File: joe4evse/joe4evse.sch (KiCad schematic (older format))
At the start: 41 parts, among them J1 USB_B_Micro, J10 Conn_01x02, J11 Conn_01x02, J12 Conn_02x06_Odd_Even, J14 Conn_01x02, J2 Conn_01x03, J3 Conn_01x03, J4 Conn_01x02, J5 Conn_01x03, J6 CONNFLY_Elec_DS1129-04-S8B0P-X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

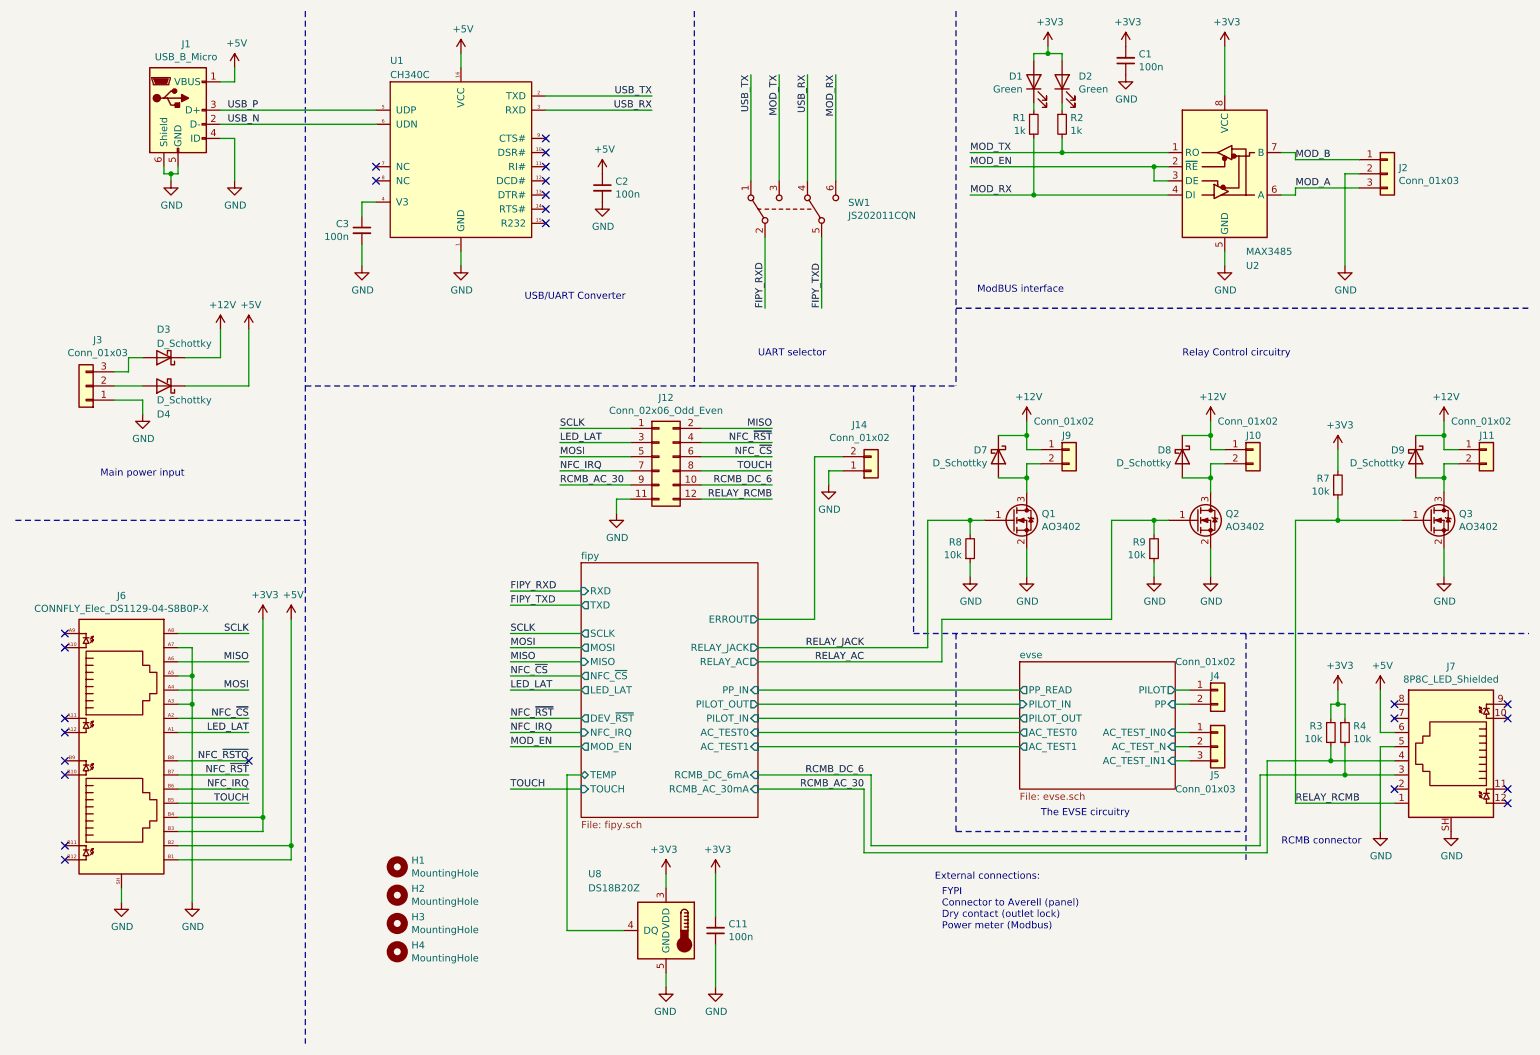
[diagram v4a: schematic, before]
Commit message: joe/{sch, pcb}: Combine AC_RELAY and RCMB output
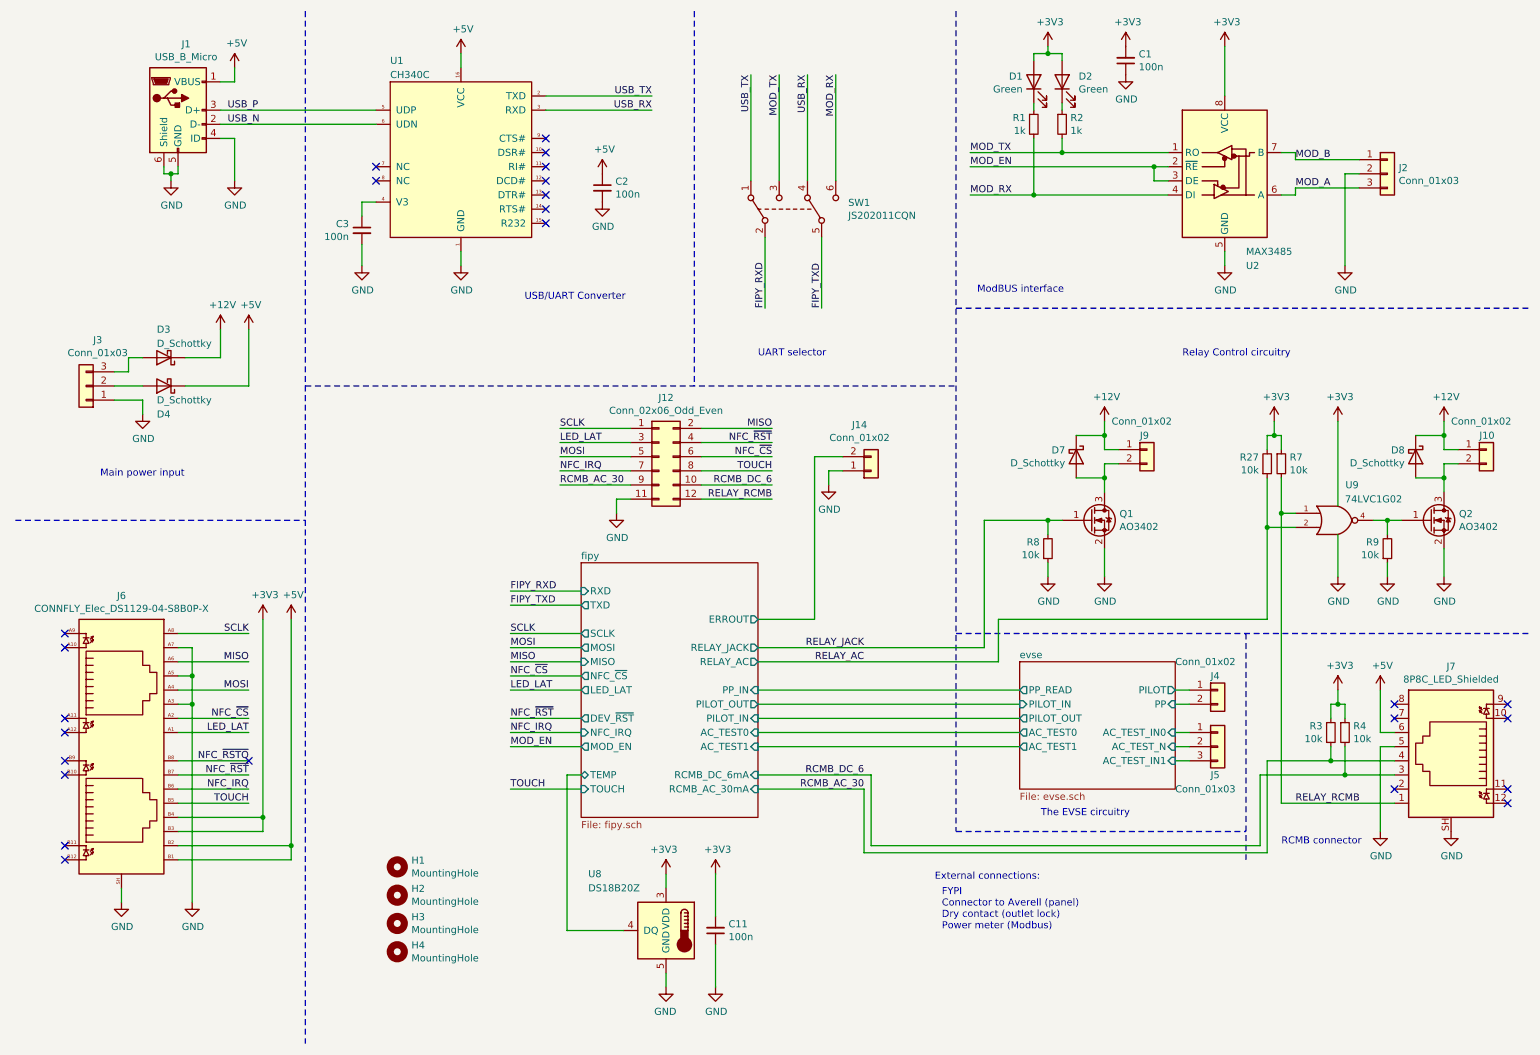
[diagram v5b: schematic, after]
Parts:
- removed D9: D_Schottky, Diode_SMD:D_SOD-123, symbol Device:D_Schottky
- removed J11: Conn_01x02, Connector_JST:JST_PH_B2B-PH-K_1x02_P2.00mm_Vertical, symbol Connector_Generic:Conn_01x02
- removed Q3: AO3402, Package_TO_SOT_SMD:SOT-23, symbol ma4evse:AO3402
- added R27: 10k, Resistor_SMD:R_0603_1608Metric, symbol Device:R_Small
- added U9: 74LVC1G02, Package_TO_SOT_SMD:SOT-353_SC-70-5, symbol 74xGxx:74LVC1G02
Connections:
- net +3V3: now also R7.1, R27.2, U9.5 (VCC); no longer R7.2
- net GND: now also U9.3 (GND)
- net RELAY_AC: now also R27.1, U9.2; no longer Q2.1 (G), R9.2
- net RELAY_RCMB: now also R7.2, U9.1; no longer R7.1
- new net: Q2.1 (G), R9.2, U9.4
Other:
- moved on the sheet: D7, D8, J10, J9, Q1, Q2, R7, R8, R9

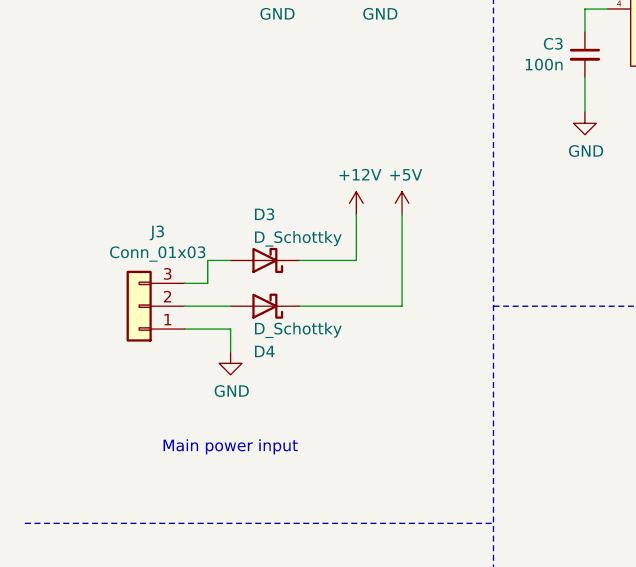
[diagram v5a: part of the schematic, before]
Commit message: joe/{sch, pcb}: Remove input shottky diodes
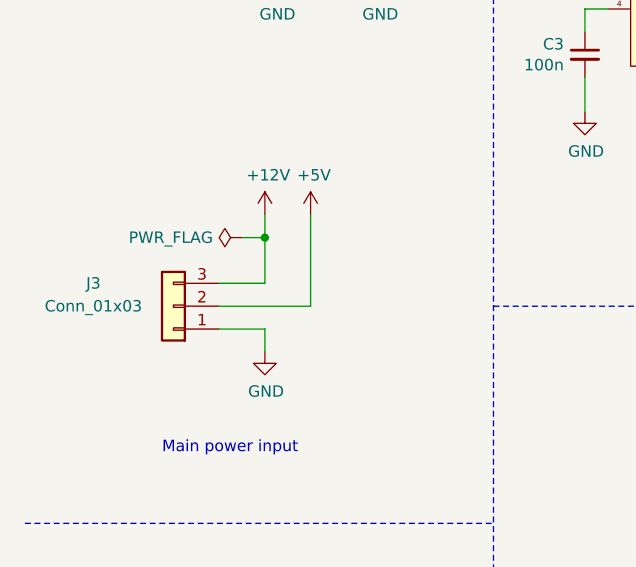
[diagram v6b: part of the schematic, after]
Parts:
- removed D3, D4: D_Schottky, Diode_SMD:D_SOD-123, symbol Device:D_Schottky
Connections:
- net +12V: now also J3.3 (Pin_3)
- net +5V: now also J3.2 (Pin_2)
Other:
- moved on the sheet: J3
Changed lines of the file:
@@
 L power:+5V #PWR016
 U 1 1 5D27C44A
-P 2150 2750
-F 0 "#PWR016" H 2150 2600 50  0001 C CNN
-F 1 "+5V" H 2165 2923 50  0000 C CNN
-F 2 "" H 2150 2750 50  0001 C CNN
-F 3 "" H 2150 2750 50  0001 C CNN
-	1    2150 2750
-	1    0    0    -1
-$EndComp
-Wire Wire Line
-	1200 3150 1400 3150
-Wire Wire Line
-	2150 3150 2150 2750
+P 1750 2750
+F 0 "#PWR016" H 1750 2600 50  0001 C CNN
+F 1 "+5V" H 1765 2923 50  0000 C CNN
+F 2 "" H 1750 2750 50  0001 C CNN
+F 3 "" H 1750 2750 50  0001 C CNN
+	1    1750 2750
+	1    0    0    -1
+$EndComp
 $Comp
 L power:GND #PWR017
 U 1 1 5D27C4DB
-P 1400 3350
-F 0 "#PWR017" H 1400 3100 50  0001 C CNN
-F 1 "GND" H 1405 3177 50  0000 C CNN
-F 2 "" H 1400 3350 50  0001 C CNN
-F 3 "" H 1400 3350 50  0001 C CNN
-	1    1400 3350
-	1    0    0    -1
-$EndComp
-Wire Wire Line
-	1200 3250 1400 3250
-Wire Wire Line
-	1400 3250 1400 3350
+P 1550 3350
+F 0 "#PWR017" H 1550 3100 50  0001 C CNN
+F 1 "GND" H 1555 3177 50  0000 C CNN
+F 2 "" H 1550 3350 50  0001 C CNN
+F 3 "" H 1550 3350 50  0001 C CNN
+	1    1550 3350
+	1    0    0    -1
+$EndComp
+Wire Wire Line
+	1350 3250 1550 3250
+Wire Wire Line
+	1550 3250 1550 3350
 Text Notes 1100 3800 0    50   ~ 0
 Main power input
@@
 	1    0    0    -1
 $EndComp
-$Comp
-L Device:D_Schottky D4
-U 1 1 5D4319B1
-P 1550 3150
-F 0 "D4" H 1600 3350 50  0000 R CNN
-F 1 "D_Schottky" H 1600 3250 50  0000 R CNN
-F 2 "Diode_SMD:D_SOD-123" H 1550 3150 50  0001 C CNN
-F 3 "~" H 1550 3150 50  0001 C CNN
-	1    1550 3150
-	-1   0    0    1
-$EndComp
-Wire Wire Line
-	1700 3150 2150 3150
 Wire Notes Line
 	5300 500  5300 3150
@@
 L Connector_Generic:Conn_01x03 J3
 U 1 1 5E273351
-P 1000 3150
-F 0 "J3" H 918 2825 50  0000 C CNN
-F 1 "Conn_01x03" H 918 2916 50  0000 C CNN
-F 2 "Connector_JST:JST_EH_B3B-EH-A_1x03_P2.50mm_Vertical" H 1000 3150 50  0001 C CNN
-F 3 "~" H 1000 3150 50  0001 C CNN
-	1    1000 3150
+P 1150 3150
+F 0 "J3" H 1500 3050 50  0000 C CNN
+F 1 "Conn_01x03" H 1500 3150 50  0000 C CNN
+F 2 "Connector_JST:JST_EH_B3B-EH-A_1x03_P2.50mm_Vertical" H 1150 3150 50  0001 C CNN
+F 3 "~" H 1150 3150 50  0001 C CNN
+	1    1150 3150
 	-1   0    0    1
 $EndComp
-$Comp
-L Device:D_Schottky D3
-U 1 1 5E2741F8
-P 1550 2950
-F 0 "D3" H 1600 2750 50  0000 R CNN
-F 1 "D_Schottky" H 1600 2850 50  0000 R CNN
-F 2 "Diode_SMD:D_SOD-123" H 1550 2950 50  0001 C CNN
-F 3 "~" H 1550 2950 50  0001 C CNN
-	1    1550 2950
-	-1   0    0    1
-$EndComp
-Wire Wire Line
-	1200 3050 1300 3050
-Wire Wire Line
-	1300 3050 1300 2950
-Wire Wire Line
-	1300 2950 1400 2950
-Wire Wire Line
-	1700 2950 1950 2950
-Wire Wire Line
-	1950 2950 1950 2750
+Wire Wire Line
+	1550 3050 1550 2850
 $Comp
 L power:+12V #PWR015
 U 1 1 5E28A95B
-P 1950 2750
-F 0 "#PWR015" H 1950 2600 50  0001 C CNN
-F 1 "+12V" H 1965 2923 50  0000 C CNN
-F 2 "" H 1950 2750 50  0001 C CNN
-F 3 "" H 1950 2750 50  0001 C CNN
-	1    1950 2750
+P 1550 2750
+F 0 "#PWR015" H 1550 2600 50  0001 C CNN
+F 1 "+12V" H 1565 2923 50  0000 C CNN
+F 2 "" H 1550 2750 50  0001 C CNN
+F 3 "" H 1550 2750 50  0001 C CNN
+	1    1550 2750
 	1    0    0    -1
 $EndComp
@@
 Wire Wire Line
 	9450 4050 9450 6100
+Wire Wire Line
+	1350 3150 1750 3150
+Wire Wire Line
+	1350 3050 1550 3050
+$Comp
+L power:PWR_FLAG #FLG0101
+U 1 1 603D27CA
+P 1450 2850
+F 0 "#FLG0101" H 1450 2925 50  0001 C CNN
+F 1 "PWR_FLAG" V 1450 2977 50  0000 L CNN
+F 2 "" H 1450 2850 50  0001 C CNN
+F 3 "~" H 1450 2850 50  0001 C CNN
+	1    1450 2850
+	0    -1   -1   0
+$EndComp
+Wire Wire Line
+	1450 2850 1550 2850
+Connection ~ 1550 2850
+Wire Wire Line
+	1550 2850 1550 2750
+Wire Wire Line
+	1750 2750 1750 3150
 $EndSCHEMATC

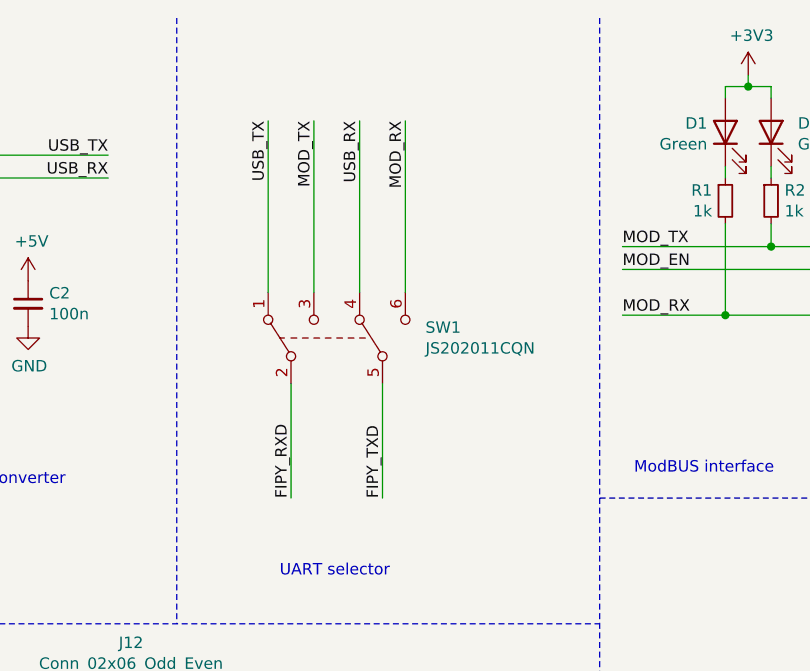
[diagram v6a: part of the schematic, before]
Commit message: joe/{sch, pcb}: Add 0r resistors in parallel of SW1 for prod boards
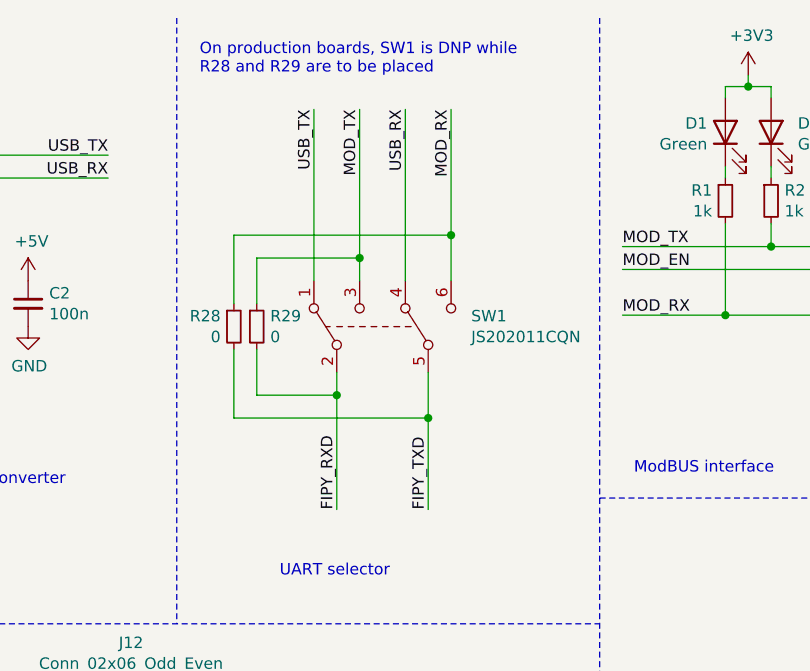
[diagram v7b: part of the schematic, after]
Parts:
- added R28, R29: 0, Resistor_SMD:R_0603_1608Metric, symbol Device:R_Small
- J1: Manufacturer (none) -> Molex; Manufacturer PN (none) -> 47346-0001
- J10, J14, J2, J3, J4, J5, J9: Manufacturer (none) -> JST
- U1: Manufacturer (none) -> WCH; Manufacturer PN (none) -> CH340C
- U2: Manufacturer (none) -> Maxim; Manufacturer PN (none) -> MAX3485
- U8: Manufacturer (none) -> Maxim
- U9: Manufacturer (none) -> Ti
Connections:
- net FIPY_RXD: now also R29.2
- net FIPY_TXD: now also R28.2
- net MOD_RX: now also R28.1
- net MOD_TX: now also R29.1
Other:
- note added: "On production boards, SW1 is DNP while\nR28 and R29 are to be placed"
- moved on the sheet: SW1
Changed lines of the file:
@@
 F 2 "Package_SO:SOIC-8_3.9x4.9mm_P1.27mm" H 9050 900 50  0001 C CNN
 F 3 "https://datasheets.maximintegrated.com/en/ds/MAX3483-MAX3491.pdf" H 9050 1650 50  0001 C CNN
+F 4 "Maxim" H 9050 1600 50  0001 C CNN "Manufacturer"
+F 5 "MAX3485" H 9050 1600 50  0001 C CNN "Manufacturer PN"
 	1    9050 1600
 	1    0    0    -1
@@
 F 2 "Connector_USB:USB_Micro-B_Molex_47346-0001" H 1800 1150 50  0001 C CNN
 F 3 "~" H 1800 1150 50  0001 C CNN
+F 4 "Molex" H 1650 1200 50  0001 C CNN "Manufacturer"
+F 5 "47346-0001" H 1650 1200 50  0001 C CNN "Manufacturer PN"
 	1    1650 1200
 	1    0    0    -1
@@
 F 2 "Package_SO:SOIC-16_3.9x9.9mm_P1.27mm" H 4050 -550 50  0001 C CNN
 F 3 "https://cdn.sparkfun.com/datasheets/Dev/Arduino/Other/CH340DS1.PDF" H 3150 1150 50  0001 C CNN
+F 4 "WCH" H 3150 1000 50  0001 C CNN "Manufacturer"
+F 5 "CH340C" H 3150 1000 50  0001 C CNN "Manufacturer PN"
 	1    3150 1000
 	1    0    0    -1
@@
 F 2 "Connector_JST:JST_EH_B3B-EH-A_1x03_P2.50mm_Vertical" H 1150 3150 50  0001 C CNN
 F 3 "~" H 1150 3150 50  0001 C CNN
+F 4 "JST" H 1150 3150 50  0001 C CNN "Manufacturer"
 	1    1150 3150
 	-1   0    0    1
@@
 F 2 "Connector_JST:JST_PH_B2B-PH-K_1x02_P2.00mm_Vertical" H 9000 5300 50  0001 C CNN
 F 3 "~" H 9000 5300 50  0001 C CNN
+F 4 "JST" H 9000 5300 50  0001 C CNN "Manufacturer"
 	1    9000 5300
 	1    0    0    -1
@@
 L ma4evse:JS202011CQN SW1
 U 1 1 5E1C964F
-P 6000 1900
-F 0 "SW1" V 6046 1512 50  0000 R CNN
-F 1 "JS202011CQN" V 5955 1512 50  0000 R CNN
-F 2 "ma4evse:JS202011CQN" H 6000 2100 50  0001 C CNN
-F 3 "~" H 6000 2100 50  0001 C CNN
-	1    6000 1900
+P 6200 1850
+F 0 "SW1" V 6246 1462 50  0000 R CNN
+F 1 "JS202011CQN" V 6155 1462 50  0000 R CNN
+F 2 "ma4evse:JS202011CQN" H 6200 2050 50  0001 C CNN
+F 3 "~" H 6200 2050 50  0001 C CNN
+	1    6200 1850
 	0    -1   -1   0
 $EndComp
 Wire Wire Line
-	6200 2100 6200 2600
-Wire Wire Line
-	5800 2100 5800 2600
-Text Label 5800 2600 1    50   ~ 0
+	6400 2050 6400 2250
+Wire Wire Line
+	6000 2050 6000 2150
+Text Label 6000 2650 1    50   ~ 0
 FIPY_RXD
-Text Label 6200 2600 1    50   ~ 0
+Text Label 6400 2650 1    50   ~ 0
 FIPY_TXD
 Wire Wire Line
-	5700 1700 5700 950
-Text Label 5700 950  3    50   ~ 0
+	5900 1650 5900 900
+Text Label 5900 900  3    50   ~ 0
 USB_TX
 Wire Wire Line
-	6100 1700 6100 950
-Text Label 6100 950  3    50   ~ 0
+	6300 1650 6300 900
+Text Label 6300 900  3    50   ~ 0
 USB_RX
 Wire Wire Line
-	5900 1700 5900 950
-Text Label 5900 950  3    50   ~ 0
+	6100 1650 6100 1550
+Text Label 6100 900  3    50   ~ 0
 MOD_TX
 Wire Wire Line
-	6300 1700 6300 950
-Text Label 6300 950  3    50   ~ 0
+	6500 1650 6500 1450
+Text Label 6500 900  3    50   ~ 0
 MOD_RX
 Wire Wire Line
@@
 F 2 "Connector_JST:JST_PH_B2B-PH-K_1x02_P2.00mm_Vertical" H 10900 3600 50  0001 C CNN
 F 3 "~" H 10900 3600 50  0001 C CNN
+F 4 "JST" H 10900 3600 50  0001 C CNN "Manufacturer"
 	1    10900 3600
 	1    0    0    -1
@@
 F 2 "Connector_JST:JST_PH_B2B-PH-K_1x02_P2.00mm_Vertical" H 8500 3600 50  0001 C CNN
 F 3 "~" H 8500 3600 50  0001 C CNN
+F 4 "JST" H 8500 3600 50  0001 C CNN "Manufacturer"
 	1    8500 3600
 	1    0    0    -1
@@
 F 2 "Connector_JST:JST_NV_B03P-NV_1x03_P5.00mm_Vertical" H 9000 5700 50  0001 C CNN
 F 3 "~" H 9000 5700 50  0001 C CNN
+F 4 "JST" H 9000 5700 50  0001 C CNN "Manufacturer"
 	1    9000 5700
 	1    0    0    -1
@@
 F 2 "Package_SO:SOIC-8_3.9x4.9mm_P1.27mm" H 4100 6750 50  0001 C CNN
 F 3 "http://datasheets.maximintegrated.com/en/ds/DS18B20.pdf" H 4950 7250 50  0001 C CNN
+F 4 "Maxim" H 5100 7000 50  0001 C CNN "Manufacturer"
 	1    5100 7000
 	-1   0    0    -1
@@
 F 2 "Connector_JST:JST_PH_B3B-PH-K_1x03_P2.00mm_Vertical" H 10200 1650 50  0001 C CNN
 F 3 "~" H 10200 1650 50  0001 C CNN
+F 4 "JST" H 10200 1650 50  0001 C CNN "Manufacturer"
 	1    10200 1650
 	1    0    0    -1
@@
 F 2 "Connector_JST:JST_PH_B2B-PH-K_1x02_P2.00mm_Vertical" H 6550 3750 50  0001 C CNN
 F 3 "~" H 6550 3750 50  0001 C CNN
+F 4 "JST" H 6550 3750 50  0001 C CNN "Manufacturer"
 	1    6550 3750
 	1    0    0    1
@@
 F 2 "Package_TO_SOT_SMD:SOT-353_SC-70-5" H 9850 4100 50  0001 C CNN
 F 3 "http://www.ti.com/lit/sg/scyt129e/scyt129e.pdf" H 9850 4100 50  0001 C CNN
+F 4 "Ti" H 9850 4100 50  0001 C CNN "Manufacturer"
 	1    9850 4100
 	1    0    0    -1
@@
 Wire Wire Line
 	1750 2750 1750 3150
+$Comp
+L Device:R_Small R28
+U 1 1 603E29DC
+P 5550 1850
+F 0 "R28" H 5492 1896 50  0000 R CNN
+F 1 "0" H 5492 1805 50  0000 R CNN
+F 2 "Resistor_SMD:R_0603_1608Metric" H 5550 1850 50  0001 C CNN
+F 3 "~" H 5550 1850 50  0001 C CNN
+	1    5550 1850
+	1    0    0    -1
+$EndComp
+Wire Wire Line
+	5650 1950 5650 2150
+Wire Wire Line
+	5650 2150 6000 2150
+Connection ~ 6000 2150
+Wire Wire Line
+	6000 2150 6000 2650
+Wire Wire Line
+	5550 1950 5550 2250
+Wire Wire Line
+	5550 2250 6400 2250
+Connection ~ 6400 2250
+Wire Wire Line
+	6400 2250 6400 2650
+Wire Wire Line
+	5650 1750 5650 1550
+Wire Wire Line
+	5650 1550 6100 1550
+Connection ~ 6100 1550
+Wire Wire Line
+	6100 1550 6100 900
+Wire Wire Line
+	5550 1750 5550 1450
+Wire Wire Line
+	5550 1450 6500 1450
+Connection ~ 6500 1450
+Wire Wire Line
+	6500 1450 6500 900
+Text Notes 5400 750  0    50   ~ 0
+On production boards, SW1 is DNP while\nR28 and R29 are to be placed
+$Comp
+L Device:R_Small R29
+U 1 1 603E30D3
+P 5650 1850
+F 0 "R29" H 5709 1896 50  0000 L CNN
+F 1 "0" H 5709 1805 50  0000 L CNN
+F 2 "Resistor_SMD:R_0603_1608Metric" H 5650 1850 50  0001 C CNN
+F 3 "~" H 5650 1850 50  0001 C CNN
+	1    5650 1850
+	1    0    0    -1
+$EndComp
 $EndSCHEMATC
